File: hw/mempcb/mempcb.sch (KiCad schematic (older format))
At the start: 26 parts

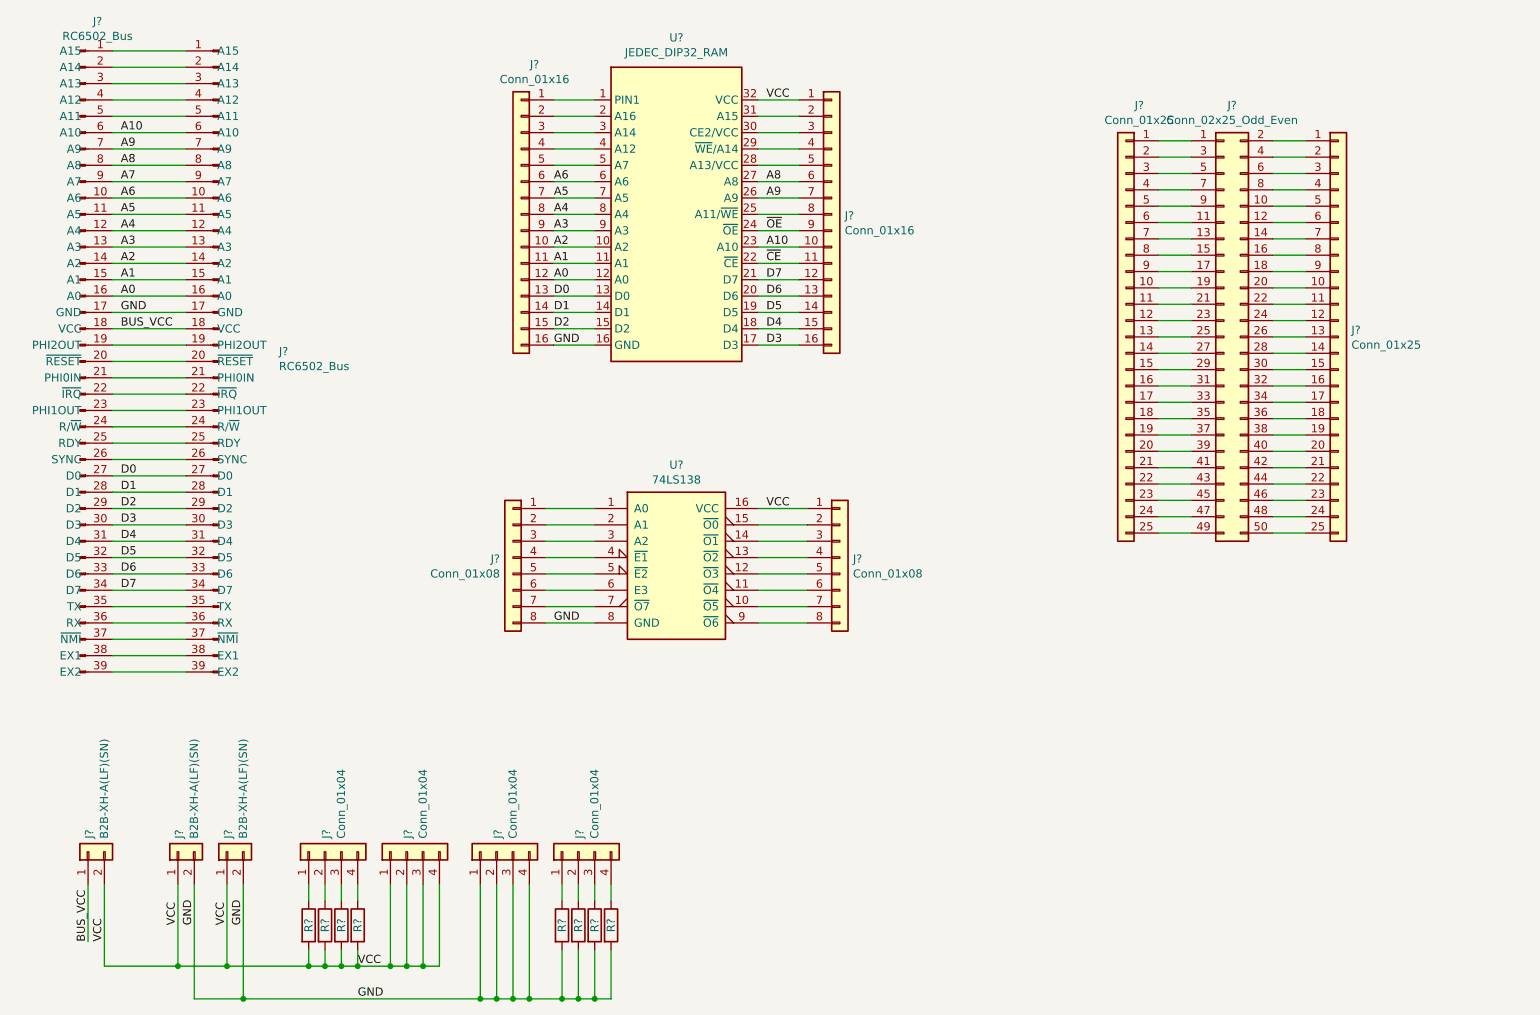
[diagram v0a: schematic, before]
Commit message: hw/mempcb/: assigned references and values
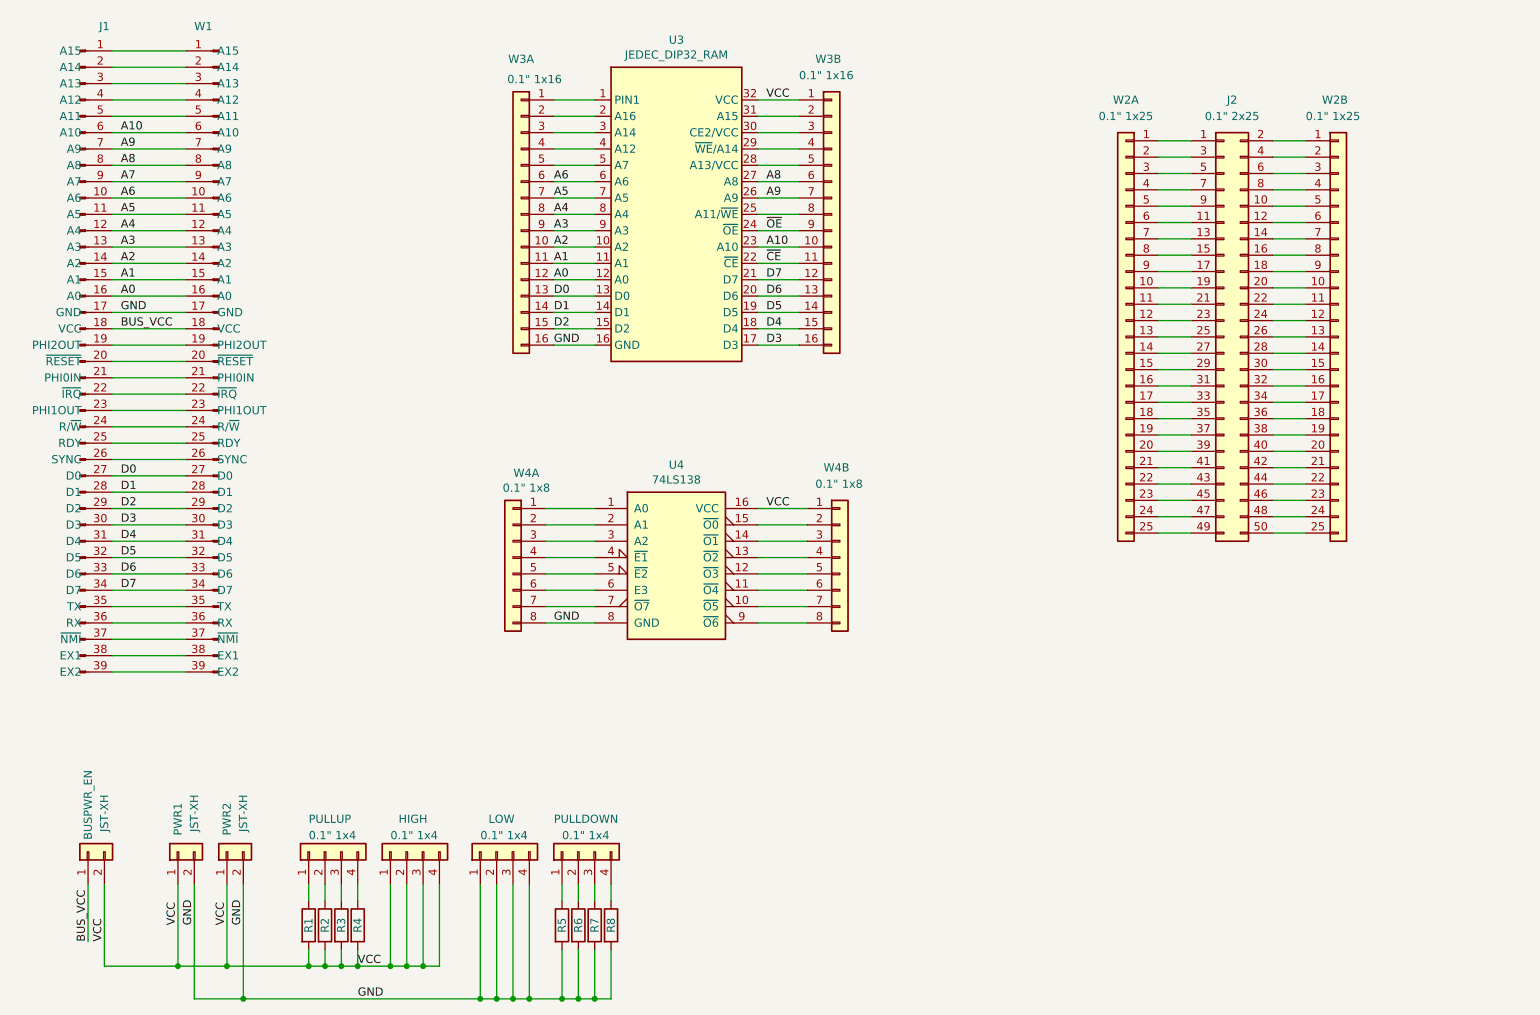
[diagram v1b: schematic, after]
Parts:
- BUSPWR_EN, PWR1, PWR2: renamed from J?; value B2B-XH-A(LF)(SN) -> JST-XH
- HIGH, LOW, PULLDOWN, PULLUP: renamed from J?; value Conn_01x04 -> 0.1\" 1x4
- J2: renamed from J?; value Conn_02x25_Odd_Even -> 0.1\" 2x25
- W2A, W2B: renamed from J?; value Conn_01x25 -> 0.1\" 1x25
- W3A, W3B: renamed from J?; value Conn_01x16 -> 0.1\" 1x16
- W4A, W4B: renamed from J?; value Conn_01x08 -> 0.1\" 1x8
- gave numbers to parts that had none: 12
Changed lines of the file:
@@
 $EndDescr
 $Comp
-L mempcb:RC6502_Bus J?
+L mempcb:RC6502_Bus J1
 U 1 1 5FE89A90
 P 1850 2900
-F 0 "J?" H 1958 4981 50  0000 C CNN
-F 1 "RC6502_Bus" H 1958 4890 50  0000 C CNN
+F 0 "J1" H 2000 4950 50  0000 C CNN
+F 1 "RC6502_Bus" H 1958 4890 50  0001 C CNN
 F 2 "" H 1850 2900 50  0001 C CNN
 F 3 "~" H 1850 2900 50  0001 C CNN
@@
 $EndComp
 $Comp
-L mempcb:RC6502_Bus J?
+L mempcb:RC6502_Bus W1
 U 1 1 5FE96F9C
 P 2700 2900
-F 0 "J?" H 2332 2961 50  0000 R CNN
-F 1 "RC6502_Bus" H 2332 2870 50  0000 R CNN
+F 0 "W1" H 2850 4950 50  0000 R CNN
+F 1 "RC6502_Bus" H 2300 4850 50  0001 R CNN
 F 2 "" H 2700 2900 50  0001 C CNN
 F 3 "~" H 2700 2900 50  0001 C CNN
@@
 $EndComp
 $Comp
-L mempcb:JEDEC_DIP32_RAM U?
+L mempcb:JEDEC_DIP32_RAM U3
 U 1 1 5FEAD713
 P 5500 2100
-F 0 "U?" H 5500 3281 50  0000 C CNN
-F 1 "JEDEC_DIP32_RAM" H 5500 3190 50  0000 C CNN
+F 0 "U3" H 5500 3267 50  0000 C CNN
+F 1 "JEDEC_DIP32_RAM" H 5500 3176 50  0000 C CNN
 F 2 "" H 5500 2100 50  0001 C CNN
 F 3 "http://www.futurlec.com/Datasheet/Memory/628128.pdf" H 5500 2100 50  0001 C CNN
@@
 $EndComp
 $Comp
-L Connector_Generic:Conn_02x25_Odd_Even J?
+L Connector_Generic:Conn_02x25_Odd_Even J2
 U 1 1 5FEB0496
 P 8850 2750
-F 0 "J?" H 8900 4167 50  0000 C CNN
-F 1 "Conn_02x25_Odd_Even" H 8900 4076 50  0000 C CNN
+F 0 "J2" H 8900 4200 50  0000 C CNN
+F 1 "0.1\" 2x25" H 8900 4100 50  0000 C CNN
 F 2 "" H 8850 2750 50  0001 C CNN
 F 3 "~" H 8850 2750 50  0001 C CNN
@@
 $EndComp
 $Comp
-L Connector_Generic:Conn_01x25 J?
+L Connector_Generic:Conn_01x25 W2A
 U 1 1 5FEB2EF1
 P 8250 2750
-F 0 "J?" H 8168 4167 50  0000 C CNN
-F 1 "Conn_01x25" H 8168 4076 50  0000 C CNN
+F 0 "W2A" H 8250 4200 50  0000 C CNN
+F 1 "0.1\" 1x25" H 8250 4100 50  0000 C CNN
 F 2 "" H 8250 2750 50  0001 C CNN
 F 3 "~" H 8250 2750 50  0001 C CNN
@@
 $EndComp
 $Comp
-L Connector_Generic:Conn_01x25 J?
+L Connector_Generic:Conn_01x25 W2B
 U 1 1 5FEC1F3E
 P 9550 2750
-F 0 "J?" H 9630 2792 50  0000 L CNN
-F 1 "Conn_01x25" H 9630 2701 50  0000 L CNN
+F 0 "W2B" H 9450 4200 50  0000 L CNN
+F 1 "0.1\" 1x25" H 9350 4100 50  0000 L CNN
 F 2 "" H 9550 2750 50  0001 C CNN
 F 3 "~" H 9550 2750 50  0001 C CNN
@@
 $EndComp
 $Comp
-L Connector_Generic:Conn_01x16 J?
+L Connector_Generic:Conn_01x16 W3A
 U 1 1 5FECEA90
 P 4550 2000
-F 0 "J?" H 4468 2917 50  0000 C CNN
-F 1 "Conn_01x16" H 4468 2826 50  0000 C CNN
+F 0 "W3A" H 4550 2950 50  0000 C CNN
+F 1 "0.1\" 1x16" H 4468 2826 50  0000 C CNN
 F 2 "" H 4550 2000 50  0001 C CNN
 F 3 "~" H 4550 2000 50  0001 C CNN
@@
 $EndComp
 $Comp
-L Connector_Generic:Conn_01x08 J?
+L Connector_Generic:Conn_01x08 W4B
 U 1 1 5FECFD2E
 P 6500 4100
-F 0 "J?" H 6580 4092 50  0000 L CNN
-F 1 "Conn_01x08" H 6580 4001 50  0000 L CNN
+F 0 "W4B" H 6400 4650 50  0000 L CNN
+F 1 "0.1\" 1x8" H 6350 4550 50  0000 L CNN
 F 2 "" H 6500 4100 50  0001 C CNN
 F 3 "~" H 6500 4100 50  0001 C CNN
@@
 $EndComp
 $Comp
-L Connector_Generic:Conn_01x08 J?
+L Connector_Generic:Conn_01x08 W4A
 U 1 1 5FED086C
 P 4500 4100
-F 0 "J?" H 4580 4092 50  0000 L CNN
-F 1 "Conn_01x08" H 4580 4001 50  0000 L CNN
+F 0 "W4A" H 4418 4617 50  0000 C CNN
+F 1 "0.1\" 1x8" H 4418 4526 50  0000 C CNN
 F 2 "" H 4500 4100 50  0001 C CNN
 F 3 "~" H 4500 4100 50  0001 C CNN
@@
 	6250 1300 6000 1300
 $Comp
-L Connector_Generic:Conn_01x16 J?
+L Connector_Generic:Conn_01x16 W3B
 U 1 1 5FECF06C
 P 6450 2000
-F 0 "J?" H 6530 1992 50  0000 L CNN
-F 1 "Conn_01x16" H 6530 1901 50  0000 L CNN
+F 0 "W3B" H 6350 2950 50  0000 L CNN
+F 1 "0.1\" 1x16" H 6250 2850 50  0000 L CNN
 F 2 "" H 6450 2000 50  0001 C CNN
 F 3 "~" H 6450 2000 50  0001 C CNN
@@
 D3
 $Comp
-L mempcb:74LS138 U?
+L mempcb:74LS138 U4
 U 1 1 5FF60AA3
 P 5500 4100
-F 0 "U?" H 5500 4667 50  0000 C CNN
+F 0 "U4" H 5500 4667 50  0000 C CNN
 F 1 "74LS138" H 5500 4576 50  0000 C CNN
 F 2 "" H 5500 4100 50  0001 C CNN
@@
 VCC
 $Comp
-L Connector_Generic:Conn_01x04 J?
+L Connector_Generic:Conn_01x04 HIGH
 U 1 1 5FED18C8
 P 3850 5900
-F 0 "J?" H 3930 5892 50  0000 L CNN
-F 1 "Conn_01x04" H 3930 5801 50  0000 L CNN
+F 0 "HIGH" V 4050 5950 50  0000 R CNN
+F 1 "0.1\" 1x4" V 3950 6000 50  0000 R CNN
 F 2 "" H 3850 5900 50  0001 C CNN
 F 3 "~" H 3850 5900 50  0001 C CNN
@@
 $EndComp
 $Comp
-L Connector_Generic:Conn_01x04 J?
+L Connector_Generic:Conn_01x04 LOW
 U 1 1 603235A5
 P 4400 5900
-F 0 "J?" H 4480 5892 50  0000 L CNN
-F 1 "Conn_01x04" H 4480 5801 50  0000 L CNN
+F 0 "LOW" V 4600 5950 50  0000 R CNN
+F 1 "0.1\" 1x4" V 4500 6000 50  0000 R CNN
 F 2 "" H 4400 5900 50  0001 C CNN
 F 3 "~" H 4400 5900 50  0001 C CNN
@@
 $EndComp
 $Comp
-L Connector_Generic:Conn_01x04 J?
+L Connector_Generic:Conn_01x04 PULLUP
 U 1 1 6032F1DA
 P 3350 5900
-F 0 "J?" H 3430 5892 50  0000 L CNN
-F 1 "Conn_01x04" H 3430 5801 50  0000 L CNN
+F 0 "PULLUP" V 3550 6000 50  0000 R CNN
+F 1 "0.1\" 1x4" V 3450 6000 50  0000 R CNN
 F 2 "" H 3350 5900 50  0001 C CNN
 F 3 "~" H 3350 5900 50  0001 C CNN
@@
 	3250 6200 3250 6100
 $Comp
-L Device:R R?
+L Device:R R2
 U 1 1 603E796E
 P 3350 6350
-F 0 "R?" V 3350 6350 50  0000 C CNN
+F 0 "R2" V 3350 6350 50  0000 C CNN
 F 1 "R" V 3350 6350 50  0001 C CNN
 F 2 "" V 3280 6350 50  0001 C CNN
@@
 	3350 6200 3350 6100
 $Comp
-L Device:R R?
+L Device:R R3
 U 1 1 60400026
 P 3450 6350
-F 0 "R?" V 3450 6350 50  0000 C CNN
+F 0 "R3" V 3450 6350 50  0000 C CNN
 F 1 "R" V 3450 6350 50  0001 C CNN
 F 2 "" V 3380 6350 50  0001 C CNN
@@
 	3450 6200 3450 6100
 $Comp
-L Device:R R?
+L Device:R R4
 U 1 1 6040C3DC
 P 3550 6350
-F 0 "R?" V 3550 6350 50  0000 C CNN
+F 0 "R4" V 3550 6350 50  0000 C CNN
 F 1 "R" V 3550 6350 50  0001 C CNN
 F 2 "" V 3480 6350 50  0001 C CNN
@@
 	3450 6600 3550 6600
 $Comp
-L Connector_Generic:Conn_01x04 J?
+L Connector_Generic:Conn_01x04 PULLDOWN
 U 1 1 6042687B
 P 4900 5900
-F 0 "J?" H 4980 5892 50  0000 L CNN
-F 1 "Conn_01x04" H 4980 5801 50  0000 L CNN
+F 0 "PULLDOWN" V 5100 6050 50  0000 R CNN
+F 1 "0.1\" 1x4" V 5000 6000 50  0000 R CNN
 F 2 "" H 4900 5900 50  0001 C CNN
 F 3 "~" H 4900 5900 50  0001 C CNN
@@
 $EndComp
 $Comp
-L Device:R R?
+L Device:R R5
 U 1 1 60426881
 P 4800 6350
-F 0 "R?" V 4800 6350 50  0000 C CNN
+F 0 "R5" V 4800 6350 50  0000 C CNN
 F 1 "R" V 4800 6350 50  0001 C CNN
 F 2 "" V 4730 6350 50  0001 C CNN
@@
 	4800 6200 4800 6100
 $Comp
-L Device:R R?
+L Device:R R6
 U 1 1 60426889
 P 4900 6350
-F 0 "R?" V 4900 6350 50  0000 C CNN
+F 0 "R6" V 4900 6350 50  0000 C CNN
 F 1 "R" V 4900 6350 50  0001 C CNN
 F 2 "" V 4830 6350 50  0001 C CNN
@@
 	4900 6200 4900 6100
 $Comp
-L Device:R R?
+L Device:R R7
 U 1 1 60426891
 P 5000 6350
-F 0 "R?" V 5000 6350 50  0000 C CNN
+F 0 "R7" V 5000 6350 50  0000 C CNN
 F 1 "R" V 5000 6350 50  0001 C CNN
 F 2 "" V 4930 6350 50  0001 C CNN
@@
 	5000 6200 5000 6100
 $Comp
-L Device:R R?
+L Device:R R8
 U 1 1 60426899
 P 5100 6350
-F 0 "R?" V 5100 6350 50  0000 C CNN
+F 0 "R8" V 5100 6350 50  0000 C CNN
 F 1 "R" V 5100 6350 50  0001 C CNN
 F 2 "" V 5030 6350 50  0001 C CNN
@@
 VCC
 $Comp
-L Device:R R?
+L Device:R R1
 U 1 1 603CD90C
 P 3250 6350
-F 0 "R?" V 3250 6350 50  0000 C CNN
+F 0 "R1" V 3250 6350 50  0000 C CNN
 F 1 "R" V 3250 6350 50  0001 C CNN
 F 2 "" V 3180 6350 50  0001 C CNN
@@
 $EndComp
 $Comp
-L Connector_Generic:Conn_01x02 J?
+L Connector_Generic:Conn_01x02 PWR1
 U 1 1 604FEFCF
 P 2450 5900
-F 0 "J?" H 2530 5892 50  0000 L CNN
-F 1 "B2B-XH-A(LF)(SN)" H 2530 5801 50  0000 L CNN
+F 0 "PWR1" H 2750 5900 50  0000 R CNN
+F 1 "JST-XH" H 2800 5800 50  0000 R CNN
 F 2 "" H 2450 5900 50  0001 C CNN
 F 3 "~" H 2450 5900 50  0001 C CNN
@@
 GND
 $Comp
-L Connector_Generic:Conn_01x02 J?
+L Connector_Generic:Conn_01x02 PWR2
 U 1 1 6051B38D
 P 2750 5900
-F 0 "J?" H 2830 5892 50  0000 L CNN
-F 1 "B2B-XH-A(LF)(SN)" H 2830 5801 50  0000 L CNN
+F 0 "PWR2" H 3050 5900 50  0000 R CNN
+F 1 "JST-XH" H 3100 5800 50  0000 R CNN
 F 2 "" H 2750 5900 50  0001 C CNN
 F 3 "~" H 2750 5900 50  0001 C CNN
@@
 BUS_VCC
 $Comp
-L Connector_Generic:Conn_01x02 J?
+L Connector_Generic:Conn_01x02 BUSPWR_EN
 U 1 1 60556D43
 P 1900 5900
-F 0 "J?" H 1980 5892 50  0000 L CNN
-F 1 "B2B-XH-A(LF)(SN)" H 1980 5801 50  0000 L CNN
+F 0 "BUSPWR_EN" H 2400 5900 50  0000 R CNN
+F 1 "JST-XH" H 2250 5800 50  0000 R CNN
 F 2 "" H 1900 5900 50  0001 C CNN
 F 3 "~" H 1900 5900 50  0001 C CNN
